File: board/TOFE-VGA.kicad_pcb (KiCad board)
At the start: 4 copper layers, 99 parts, among them P301 TOFE I2C, P302 TOFE-8X, P303 DEBUG, P401 AD9984 I2C, P501 VGA RX I2C 3v, P502 VGA TX I2C 3v, P503 VGA RX I2C 5v, P504 VGA TX I2C 5v, P505 DE-15, P506 DE-15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

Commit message: Misc things not commited yet
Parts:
- moved P505 7.00 mm to (62.2, 127.0)
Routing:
- net /TOFE-VGA/AD9984/HSYNC0: track 0.00 -> 44.7 mm
- net Net-(D301-Pad1): track 0.00 -> 28.4 mm
- net GND: track 0.00 -> 15.2 mm
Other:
- net class Default: clearance 0.254 -> 0.25; trace_width 0.254 -> 0.25; via_dia 0.889 -> 0.7; via_drill 0.635 -> 0.3
- rule trace_clearance: 0.254 -> 0.25
- rule trace_min: 0.254 -> 0.25
- rule via_min_drill: 0.508 -> 0.3
- rule via_min_size: 0.889 -> 0.7
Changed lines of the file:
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@@
   (general
     (links 328)
-    (no_connects 322)
-    (area 15.671 46.895999 230.304001 253.379)
+    (no_connects 321)
+    (area -7.154 46.895999 230.304001 249.129)
     (thickness 1.6)
     (drawings 3)
-    (tracks 0)
+    (tracks 19)
     (zones 0)
     (modules 99)
@@
   )
   (setup
-    (last_trace_width 0.254)
-    (trace_clearance 0.254)
+    (last_trace_width 0.25)
+    (user_trace_width 0.25)
+    (user_trace_width 0.5)
+    (user_trace_width 1)
+    (user_trace_width 1.25)
+    (user_trace_width 1.5)
+    (trace_clearance 0.25)
     (zone_clearance 0.508)
     (zone_45_only no)
-    (trace_min 0.254)
+    (trace_min 0.25)
     (segment_width 0.2)
     (edge_width 0.1)
-    (via_size 0.889)
-    (via_drill 0.635)
-    (via_min_size 0.889)
-    (via_min_drill 0.508)
+    (via_size 0.7)
+    (via_drill 0.3)
+    (via_min_size 0.7)
+    (via_min_drill 0.3)
     (uvia_size 0.508)
     (uvia_drill 0.127)
@@
   (net 114 "Net-(U401-Pad16)")
   (net_class Default "This is the default net class."
-    (clearance 0.254)
-    (trace_width 0.254)
-    (via_dia 0.889)
-    (via_drill 0.635)
+    (clearance 0.25)
+    (trace_width 0.25)
+    (via_dia 0.7)
+    (via_drill 0.3)
     (uvia_dia 0.508)
     (uvia_drill 0.127)
@@
   )
   (module DE-15:TE-1-1734530-1 (layer F.Cu)
-    (at 62.2 120 270)
+    (at 62.2 127 270)
     (fp_text reference P505 (at 0 -4 270) (layer F.SilkS)
       (effects (font (size 1 1) (thickness 0.15)))
@@
   (gr_line (start 161.2 60) (end 62.2 60) (angle 90) (layer Cmts.User) (width 0.2))
   (gr_line (start 161.2 159) (end 161.2 60) (angle 90) (layer Cmts.User) (width 0.2))
+  (segment (start 73.63 130.17) (end 73.63 132.46) (width 0.5) (layer In2.Cu) (net 4))
+  (segment (start 73.63 127.88) (end 73.63 130.17) (width 0.5) (layer In2.Cu) (net 4))
+  (segment (start 73.63 123.3) (end 75.03 123.3) (width 0.5) (layer In2.Cu) (net 4))
+  (segment (start 75.03 123.3) (end 76.17 122.16) (width 0.5) (layer In2.Cu) (net 4))
+  (segment (start 73.63 88.17) (end 73.63 85.88) (width 1) (layer In2.Cu) (net 4))
+  (segment (start 73.63 90.46) (end 73.63 88.17) (width 1) (layer In2.Cu) (net 4))
+  (segment (start 73.63 81.3) (end 74.77 80.16) (width 1) (layer In2.Cu) (net 4))
+  (segment (start 74.77 80.16) (end 76.17 80.16) (width 1) (layer In2.Cu) (net 4))
+  (segment (start 109.89938 155.3) (end 109.89938 147.00064) (width 0.5) (layer F.Cu) (net 24))
+  (segment (start 109.89938 147.00064) (end 110.2 146.70002) (width 0.5) (layer F.Cu) (net 24))
+  (segment (start 108.90116 155.3) (end 108.90116 147.99886) (width 0.5) (layer F.Cu) (net 24))
+  (segment (start 108.90116 147.99886) (end 110.2 146.70002) (width 0.5) (layer F.Cu) (net 24))
+  (segment (start 107.9004 155.3) (end 107.9004 147.349) (width 0.5) (layer F.Cu) (net 24))
+  (segment (start 107.9004 147.349) (end 108.54938 146.70002) (width 0.5) (layer F.Cu) (net 24))
+  (segment (start 108.54938 146.70002) (end 110.2 146.70002) (width 0.5) (layer F.Cu) (net 24))
+  (segment (start 71.09 126.74) (end 67.865001 123.515001) (width 0.25) (layer B.Cu) (net 93))
+  (segment (start 67.865001 123.515001) (end 67.865001 87.964999) (width 0.25) (layer B.Cu) (net 93))
+  (segment (start 67.865001 87.964999) (end 70.090001 85.739999) (width 0.25) (layer B.Cu) (net 93))
+  (segment (start 70.090001 85.739999) (end 71.09 84.74) (width 0.25) (layer B.Cu) (net 93))
 )

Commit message: Adding new parts.
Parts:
- added C408: 47n, Resistors_SMD:R_0805_HandSoldering, F.Cu at (128.0, 72.6)
- added C409: 10n, Resistors_SMD:R_0805_HandSoldering, F.Cu at (121.3, 72.9)
- added C410: 82n, Resistors_SMD:R_0805_HandSoldering, F.Cu at (109.4, 73.0)
- added C411: 8.2n, Resistors_SMD:R_0805_HandSoldering, F.Cu at (100.2, 73.5)
- added L404: FERRITE, Resistors_SMD:R_0805_HandSoldering, F.Cu at (133.2, 77.7)
- added L405: FERRITE, Resistors_SMD:R_0805_HandSoldering, F.Cu at (141.1, 73.8)
- added L406: FERRITE, Resistors_SMD:R_0805_HandSoldering, F.Cu at (141.9, 78.6)
- added P601: 3-RCA, 3-RCA:MR-100H, F.Cu at (115.7, 61.6)
- added R414: 1K, Resistors_SMD:R_0805_HandSoldering, F.Cu at (116.2, 76.8)
- added R415: 2k2, Resistors_SMD:R_0805_HandSoldering, F.Cu at (126.1, 76.8)
- added R416: 2K2, Resistors_SMD:R_0805_HandSoldering, F.Cu at (135.4, 74.2)
- C405: value 10n -> 47n
- C406: value 82n -> 47n
- C407: value 8.2n -> 47n
- R404: value 1K -> 75R
- R405, R406: value 10K -> 75R
- R407: value 1K5 -> 1K
- R408, R409: value 1K -> 10K
- R410: value 1K -> 1K5
- R412: value 2k2 -> 1K
- R413: value 2K2 -> 1K
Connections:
- C201 pad 2: Net-(C201-Pad2) -> GNDA
- C203 pad 2: Net-(C201-Pad2) -> GNDA
- C205 pad 2: Net-(C201-Pad2) -> GNDA
- C207 pad 2: Net-(C201-Pad2) -> GNDA
- C209 pad 2: Net-(C201-Pad2) -> GNDA
- C211 pad 2: Net-(C201-Pad2) -> GNDA
- C213 pad 2: Net-(C201-Pad2) -> GNDA
- C216 pad 2: Net-(C216-Pad2) -> GND
- C218 pad 2: Net-(C216-Pad2) -> GND
- C219 pad 2: Net-(C216-Pad2) -> GND
- C220 pad 2: Net-(C216-Pad2) -> GND
- C221 pad 2: Net-(C216-Pad2) -> GND
- C403 pad 2: Net-(C402-Pad2) -> Net-(C403-Pad2)
- C404 pad 2: Net-(C404-Pad2) -> Net-(C403-Pad2)
- C406 pad 1: PVD -> Net-(C406-Pad1)
- C406 pad 2: Net-(C406-Pad2) -> Net-(C405-Pad2)
- C407 pad 1: PVD -> Net-(C407-Pad1)
- L402 pad 1: /TOFE-VGA/AD9984/VGA_G -> /TOFE-VGA/AD9984/COMP_Pb
- L403 pad 1: /TOFE-VGA/AD9984/VGA_R -> /TOFE-VGA/AD9984/VGA_G
- L403 pad 2: Net-(C404-Pad2) -> Net-(C403-Pad2)
- P401 pad 1: +3V3 -> Net-(P401-Pad1)
- P505 pad 10: GND -> GNDA
- P505 pad 5: GND -> GNDA
- P505 pad 6: GND -> GNDA
- P505 pad 7: GND -> GNDA
- P505 pad 8: GND -> GNDA
- P506 pad 10: GND -> GNDA
- P506 pad 5: GND -> GNDA
- P506 pad 6: GND -> GNDA
- P506 pad 7: GND -> GNDA
- P506 pad 8: GND -> GNDA
- R203 pad 2: Net-(C201-Pad2) -> GNDA
- R205 pad 2: Net-(C201-Pad2) -> GNDA
- R207 pad 2: Net-(C216-Pad2) -> GND
- R209 pad 2: Net-(C216-Pad2) -> GND
- R401 pad 2: GND -> GNDA
- R402 pad 2: GND -> GNDA
- R403 pad 1: Net-(C404-Pad2) -> Net-(C403-Pad2)
- R403 pad 2: GND -> GNDA
- R404 pad 1: Net-(R404-Pad1) -> Net-(C405-Pad2)
- R404 pad 2: GND -> GNDA
- R405 pad 1: +3V3 -> Net-(C407-Pad2)
- R405 pad 2: /TOFE-VGA/AD9984/VSOUT -> GNDA
- R406 pad 1: /TOFE-VGA/AD9984/VSOUT -> Net-(C408-Pad2)
- R406 pad 2: GND -> GNDA
- R407 pad 1: Net-(C407-Pad2) -> Net-(R407-Pad1)
- R407 pad 2: Net-(C406-Pad2) -> GNDA
- R408 pad 1: Net-(R408-Pad1) -> +3V3
- R408 pad 2: GND -> /TOFE-VGA/AD9984/VSOUT
- R409 pad 1: Net-(R409-Pad1) -> /TOFE-VGA/AD9984/VSOUT
- R410 pad 1: GND -> Net-(C411-Pad2)
- R410 pad 2: Net-(R410-Pad2) -> Net-(C410-Pad2)
- R411 pad 1: GND -> Net-(R411-Pad1)
- R411 pad 2: Net-(R411-Pad2) -> GND
- R412 pad 1: +3V3 -> Net-(R412-Pad1)
- R412 pad 2: /TOFE-VGA/AD9984/SCL_AD9984 -> GND
- R413 pad 1: +3V3 -> GND
- R413 pad 2: /TOFE-VGA/AD9984/SDA_AD9984 -> Net-(R413-Pad2)
- TP401 pad 1: Net-(R404-Pad1) -> Net-(R407-Pad1)
- TP403 pad 1: Net-(R408-Pad1) -> Net-(R411-Pad1)
- TP404 pad 1: Net-(R409-Pad1) -> Net-(R412-Pad1)
- U201 pad 1: Net-(C201-Pad2) -> GNDA
- U201 pad 2: Net-(C201-Pad2) -> GNDA
- U202 pad 1: Net-(C216-Pad2) -> GND
- U202 pad 2: Net-(C216-Pad2) -> GND
- U401 pad 10: Net-(U401-Pad10) -> Net-(C405-Pad1)
- U401 pad 11: GND -> GNDA
- U401 pad 12: Net-(U401-Pad12) -> Net-(C406-Pad1)
- U401 pad 14: Net-(C404-Pad1) -> Net-(C407-Pad1)
- U401 pad 15: GND -> GNDA
- U401 pad 17: Net-(R404-Pad1) -> Net-(R407-Pad1)
- U401 pad 18: Net-(C405-Pad2) -> Net-(C409-Pad2)
- U401 pad 20: Net-(C405-Pad1) -> Net-(C409-Pad1)
- U401 pad 3: GND -> GNDA
- U401 pad 4: Net-(U401-Pad4) -> Net-(C402-Pad1)
- U401 pad 6: Net-(C402-Pad1) -> Net-(C403-Pad1)
- U401 pad 64: +3V3 -> Net-(P401-Pad1)
- U401 pad 68: Net-(R411-Pad2) -> Net-(R414-Pad2)
- U401 pad 69: Net-(R410-Pad2) -> Net-(R413-Pad2)
- U401 pad 7: GND -> GNDA
- U401 pad 72: Net-(R409-Pad1) -> Net-(R412-Pad1)
- U401 pad 73: Net-(R408-Pad1) -> Net-(R411-Pad1)
- U401 pad 78: Net-(C407-Pad2) -> Net-(C411-Pad2)
- U401 pad 8: Net-(C403-Pad1) -> Net-(C404-Pad1)
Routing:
- net GNDA: track 0.00 -> 15.2 mm
- net GND: track 15.2 -> 0.00 mm
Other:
- board outline added: 46 x 3 mm

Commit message: Initial PCB design by Phyllis.
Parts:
- added C1: C, Capacitors_SMD:C_0805_HandSoldering, F.Cu at (94.1, 120.1)
- moved R508 189.7 mm to (89.6, 76.8), turned to 270 degrees
- moved P502 184.1 mm to (103.0, 79.5), turned to 90 degrees
- moved R506 176.7 mm to (89.6, 81.5), turned to 90 degrees
- moved U502 176.2 mm to (94.0, 79.2), turned to 180 degrees
- moved R502 164.5 mm to (98.1, 77.1), turned to 270 degrees
- moved P504 158.4 mm to (84.7, 79.6), turned to 270 degrees
- moved R504 154.7 mm to (98.1, 81.5), turned to 90 degrees
- moved R507 144.9 mm to (89.9, 124.9), turned to 270 degrees
- moved C216 129.0 mm to (125.8, 83.9)
- moved R505 127.9 mm to (89.9, 129.5), turned to 90 degrees
- moved P503 126.6 mm to (84.9, 126.6), turned to 270 degrees
- moved U202 125.9 mm to (131.7, 84.1)
- moved R206 123.0 mm to (135.9, 84.3)
- moved C218 118.4 mm to (139.9, 83.8), turned to 270 degrees
- moved R207 117.7 mm to (134.5, 81.0), turned to 180 degrees
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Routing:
- net GND: track 0.00 -> 192.7 mm, vias 0 -> 66
- net /TOFE-VGA/AD9984/VSYNC0: track 0.00 -> 153.7 mm
- net +12V: track 0.00 -> 150.4 mm, vias 0 -> 5
- net /TOFE-VGA/AD9984/HSYNC0: track 44.7 -> 159.9 mm, vias 0 -> 1
- net +5V: track 0.00 -> 100.0 mm, vias 0 -> 8
- net /TOFE-VGA/TOFE/EN_VGA_TX: track 0.00 -> 97.5 mm, vias 0 -> 1
- net /TOFE-VGA/TOFE/SDA_VGA_TX: track 0.00 -> 91.6 mm, vias 0 -> 1
- net /TOFE-VGA/TOFE/SCL_VGA_TX: track 0.00 -> 87.5 mm, vias 0 -> 1
- net /TOFE-VGA/AD9984/VGA_R: track 0.00 -> 78.4 mm, vias 0 -> 2
- net /TOFE-VGA/AD9984/VGA_G: track 0.00 -> 78.3 mm, vias 0 -> 2
- net PRNST: track 0.00 -> 77.3 mm, vias 0 -> 2
- net /TOFE-VGA/AD9984/VGA_B: track 0.00 -> 76.3 mm, vias 0 -> 1
- net /TOFE-VGA/AD9984/SCL_AD9984: track 0.00 -> 75.8 mm, vias 0 -> 1
- net /TOFE-VGA/AD9984/SDA_AD9984: track 0.00 -> 72.4 mm, vias 0 -> 1
- net GNDA: track 15.2 -> 83.1 mm, vias 0 -> 22
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- added copper zone on In2.Cu, net +3V3
- added copper zone on In1.Cu, net GND
- added copper zone on In1.Cu, net GNDA
- added copper zone on In2.Cu, net PVD
- added copper zone on In2.Cu, net VD
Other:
- net class Default: clearance 0.25 -> 0.127; trace_width 0.25 -> 0.127; via_dia 0.7 -> 0.61; via_drill 0.3 -> 0.305
- rule trace_clearance: 0.25 -> 0.127
- rule trace_min: 0.25 -> 0.127
- rule via_min_drill: 0.3 -> 0.305
- rule via_min_size: 0.7 -> 0.61
- board text added: "N/C"

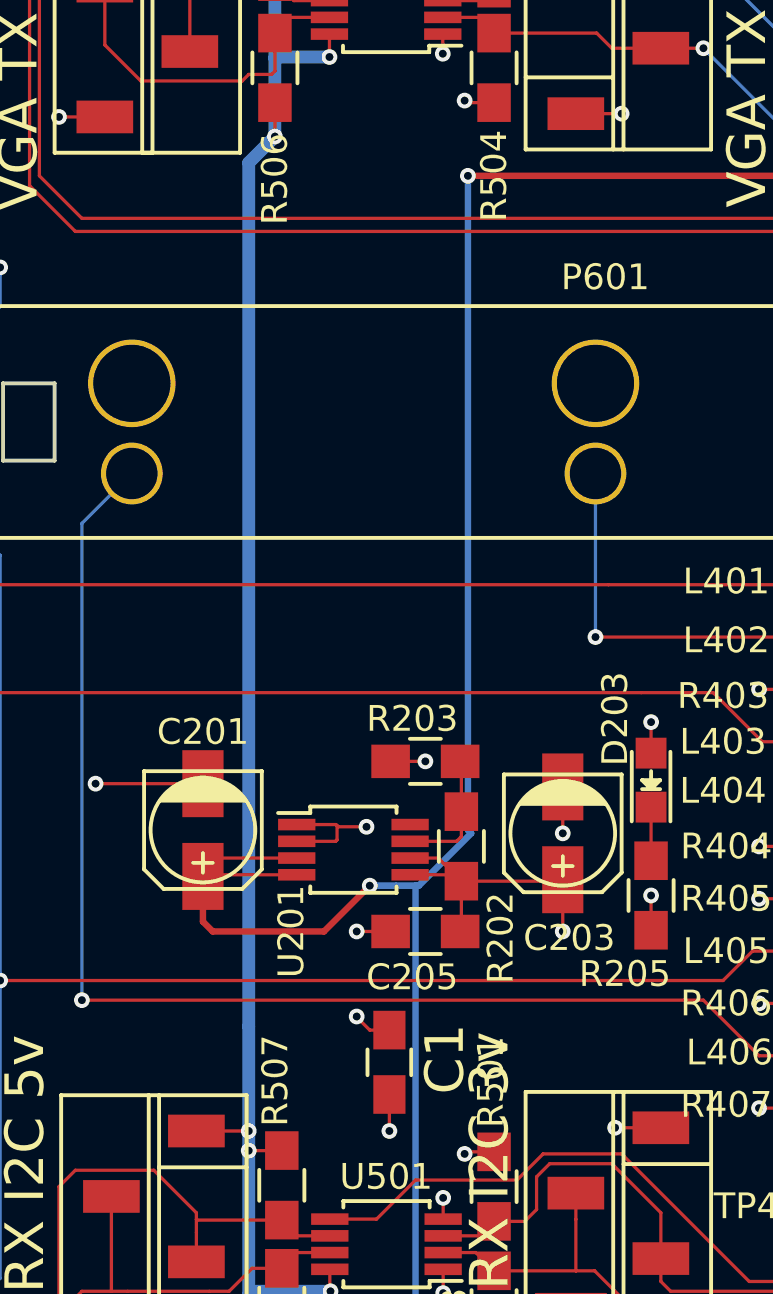
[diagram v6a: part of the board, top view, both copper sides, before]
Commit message: Adding a way to disconnect the output from the input.
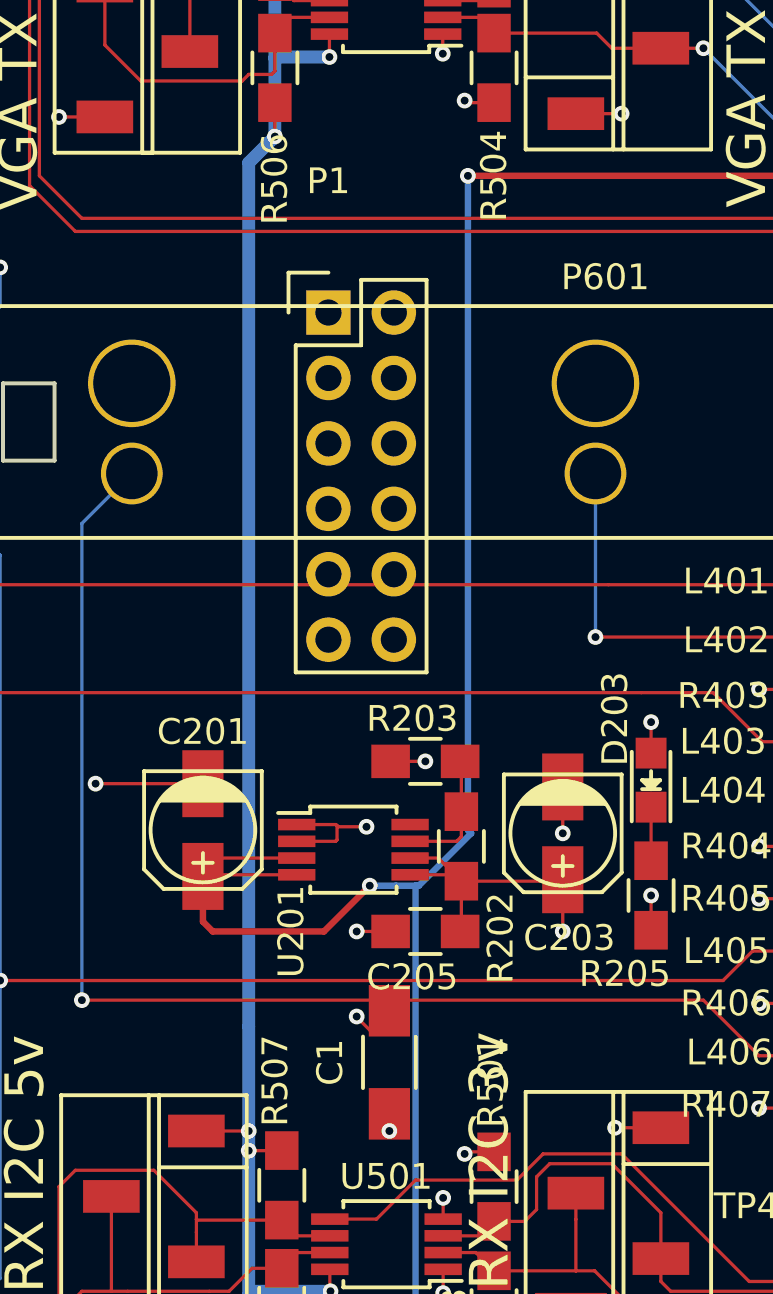
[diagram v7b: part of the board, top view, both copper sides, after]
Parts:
- added P1: CONN_02X06, Pin_Headers:Pin_Header_Straight_2x06, F.Cu at (91.7, 91.0)
- C1: footprint Capacitors_SMD:C_0805_HandSoldering -> Capacitors_SMD:C_1206_HandSoldering
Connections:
- L401 pad 1: /TOFE-VGA/AD9984/VGA_B -> /TOFE-VGA/VGA/VGAIN_B
- L403 pad 1: /TOFE-VGA/AD9984/VGA_G -> /TOFE-VGA/VGA/VGAIN_G
- L405 pad 1: /TOFE-VGA/AD9984/VGA_R -> /TOFE-VGA/VGA/VGAIN_R
- P505 pad 1: /TOFE-VGA/AD9984/VGA_R -> /TOFE-VGA/VGA/VGAIN_R
- P505 pad 14: /TOFE-VGA/AD9984/VSYNC0 -> /TOFE-VGA/VGA/VGAIN_VSYNC0
- P505 pad 2: /TOFE-VGA/AD9984/VGA_G -> /TOFE-VGA/VGA/VGAIN_G
- P505 pad 3: /TOFE-VGA/AD9984/VGA_B -> /TOFE-VGA/VGA/VGAIN_B
- P506 pad 1: /TOFE-VGA/AD9984/VGA_R -> /TOFE-VGA/VGA/VGAOUT_R
- P506 pad 13: /TOFE-VGA/AD9984/HSYNC0 -> /TOFE-VGA/VGA/VGAOUT_HSYNC0
- P506 pad 14: /TOFE-VGA/AD9984/VSYNC0 -> /TOFE-VGA/VGA/VGAOUT_VSYNC0
- P506 pad 2: /TOFE-VGA/AD9984/VGA_G -> /TOFE-VGA/VGA/VGAOUT_G
- P506 pad 3: /TOFE-VGA/AD9984/VGA_B -> /TOFE-VGA/VGA/VGAOUT_B
- U401 pad 71: /TOFE-VGA/AD9984/VSYNC0 -> /TOFE-VGA/VGA/VGAIN_VSYNC0
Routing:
- net /TOFE-VGA/AD9984/VSYNC0: track 153.7 -> 0.00 mm
- net /TOFE-VGA/VGA/VGAIN_VSYNC0: track 0.00 -> 131.8 mm
- net /TOFE-VGA/AD9984/VGA_R: track 78.4 -> 0.00 mm, vias 2 -> 0
- net /TOFE-VGA/AD9984/VGA_G: track 78.3 -> 0.00 mm, vias 2 -> 0
- net /TOFE-VGA/AD9984/VGA_B: track 76.3 -> 0.00 mm, vias 1 -> 0
- net /TOFE-VGA/VGA/VGAIN_G: track 0.00 -> 76.1 mm, vias 0 -> 2
- net /TOFE-VGA/VGA/VGAIN_B: track 0.00 -> 74.1 mm, vias 0 -> 1
- net /TOFE-VGA/VGA/VGAIN_R: track 0.00 -> 74.0 mm, vias 0 -> 1
- net /TOFE-VGA/VGA/VGAOUT_VSYNC0: track 0.00 -> 21.9 mm
- net (no net): track 30.1 -> 42.2 mm, vias 0 -> 1
- net /TOFE-VGA/AD9984/G9: track 44.4 -> 32.3 mm, vias 2 -> 1
- net /TOFE-VGA/AD9984/HSYNC0: track 159.9 -> 155.2 mm, vias 1 -> 0
- net /TOFE-VGA/VGA/VGAOUT_HSYNC0: track 0.00 -> 4.69 mm, vias 0 -> 1
- net /TOFE-VGA/VGA/VGAOUT_R: track 0.00 -> 4.34 mm, vias 0 -> 1
- net /TOFE-VGA/VGA/VGAOUT_G: track 0.00 -> 2.20 mm
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
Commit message: Couple more GND<->GNDA coupling capacitors.
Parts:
- added C2: C, Capacitors_SMD:C_1206_HandSoldering, F.Cu at (126.2, 73.8)
- added C3: C, Capacitors_SMD:C_1206_HandSoldering, F.Cu at (126.2, 68.8)
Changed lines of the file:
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@@
 (kicad_pcb (version 4) (host pcbnew 4.0.2+e4-6225~38~ubuntu14.04.1-stable)
   (general
-    (links 356)
-    (no_connects 54)
+    (links 360)
+    (no_connects 56)
     (area 0 0 0 0)
     (thickness 1.6)
@@
     (tracks 1443)
     (zones 0)
-    (modules 112)
+    (modules 114)
     (nets 127)
   )
@@
       (net 98 GNDA))
     (model Capacitors_SMD.3dshapes/C_1206_HandSoldering.wrl
+      (at (xyz 0 0 0))
+      (scale (xyz 1 1 1))
+      (rotate (xyz 0 0 0))
+    )
+  )
+  (module Capacitors_SMD:C_1206_HandSoldering (layer F.Cu)
+    (at 126.225 73.775)
+    (descr "Capacitor SMD 1206, hand soldering")
+    (tags "capacitor 1206")
+    (attr smd)
+    (fp_text reference C2 (at 0 -2.3) (layer F.SilkS)
+      (effects (font (size 1 1) (thickness 0.15)))
+    )
+    (fp_text value C (at 0 2.3) (layer F.Fab)
+      (effects (font (size 1 1) (thickness 0.15)))
+    )
+    (fp_line (start -3.3 -1.15) (end 3.3 -1.15) (layer F.CrtYd) (width 0.05))
+    (fp_line (start -3.3 1.15) (end 3.3 1.15) (layer F.CrtYd) (width 0.05))
+    (fp_line (start -3.3 -1.15) (end -3.3 1.15) (layer F.CrtYd) (width 0.05))
+    (fp_line (start 3.3 -1.15) (end 3.3 1.15) (layer F.CrtYd) (width 0.05))
+    (fp_line (start 1 -1.025) (end -1 -1.025) (layer F.SilkS) (width 0.15))
+    (fp_line (start -1 1.025) (end 1 1.025) (layer F.SilkS) (width 0.15))
+    (pad 1 smd rect (at -2 0) (size 2 1.6) (layers F.Cu F.Paste F.Mask)
+      (net 3 GND))
+    (pad 2 smd rect (at 2 0) (size 2 1.6) (layers F.Cu F.Paste F.Mask)
+      (net 98 GNDA))
+    (model Capacitors_SMD.3dshapes/C_1206_HandSoldering.wrl
+      (at (xyz 0 0 0))
+      (scale (xyz 1 1 1))
+      (rotate (xyz 0 0 0))
+    )
+  )
+  (module Capacitors_SMD:C_1206_HandSoldering (layer F.Cu)
+    (at 126.15 68.8)
+    (descr "Capacitor SMD 1206, hand soldering")
+    (tags "capacitor 1206")
+    (attr smd)
+    (fp_text reference C3 (at 0 -2.3) (layer F.SilkS)
+      (effects (font (size 1 1) (thickness 0.15)))
+    )
+    (fp_text value C (at 0 2.3) (layer F.Fab)
+      (effects (font (size 1 1) (thickness 0.15)))
+    )
+    (fp_line (start -3.3 -1.15) (end 3.3 -1.15) (layer F.CrtYd) (width 0.05))
+    (fp_line (start -3.3 1.15) (end 3.3 1.15) (layer F.CrtYd) (width 0.05))
+    (fp_line (start -3.3 -1.15) (end -3.3 1.15) (layer F.CrtYd) (width 0.05))
+    (fp_line (start 3.3 -1.15) (end 3.3 1.15) (layer F.CrtYd) (width 0.05))
+    (fp_line (start 1 -1.025) (end -1 -1.025) (layer F.SilkS) (width 0.15))
+    (fp_line (start -1 1.025) (end 1 1.025) (layer F.SilkS) (width 0.15))
+    (pad 1 smd rect (at -2 0) (size 2 1.6) (layers F.Cu F.Paste F.Mask)
+      (net 3 GND))
+    (pad 2 smd rect (at 2 0) (size 2 1.6) (layers F.Cu F.Paste F.Mask)
+      (net 98 GNDA))
+    (model Capacitors_SMD.3dshapes/C_1206_HandSoldering.wrl
